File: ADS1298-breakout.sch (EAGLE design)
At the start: 33 parts, among them IC2 TPS73250DBVT, IC3 TPS73233DBVT

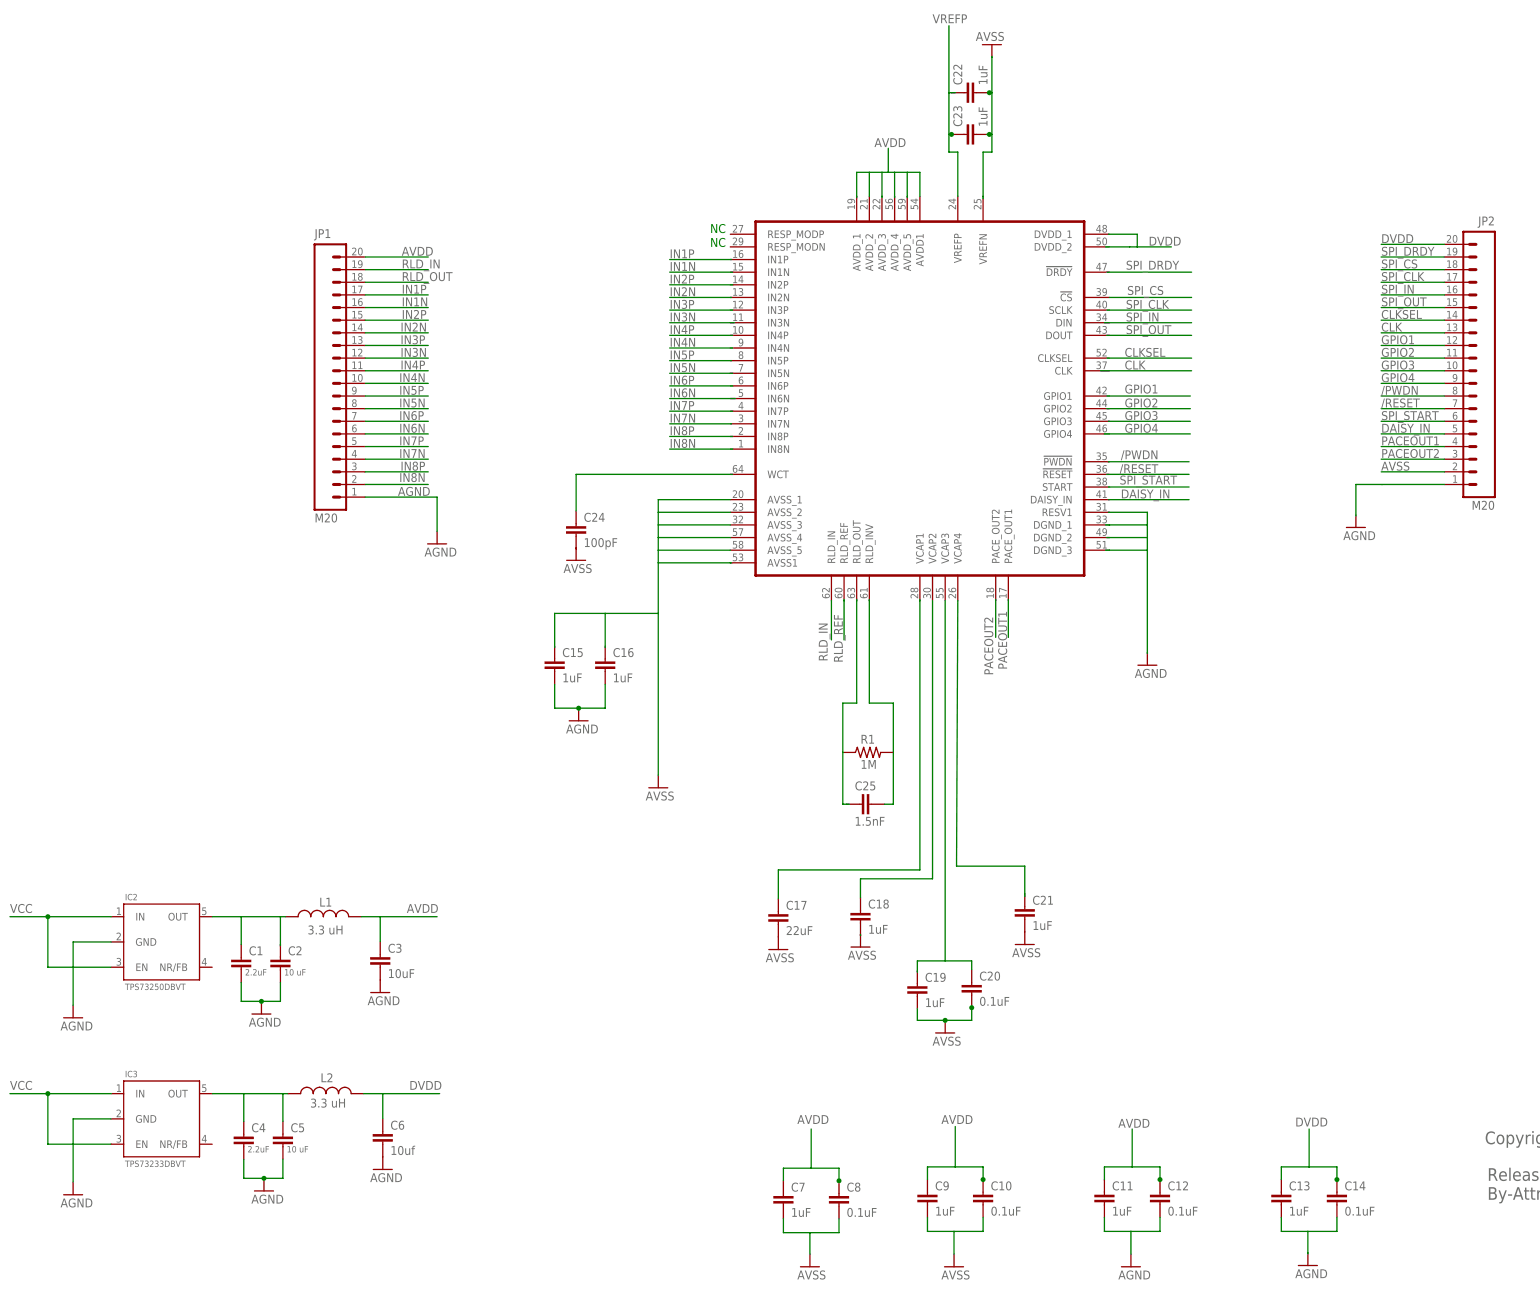
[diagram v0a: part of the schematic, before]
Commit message: schematic passes ERC
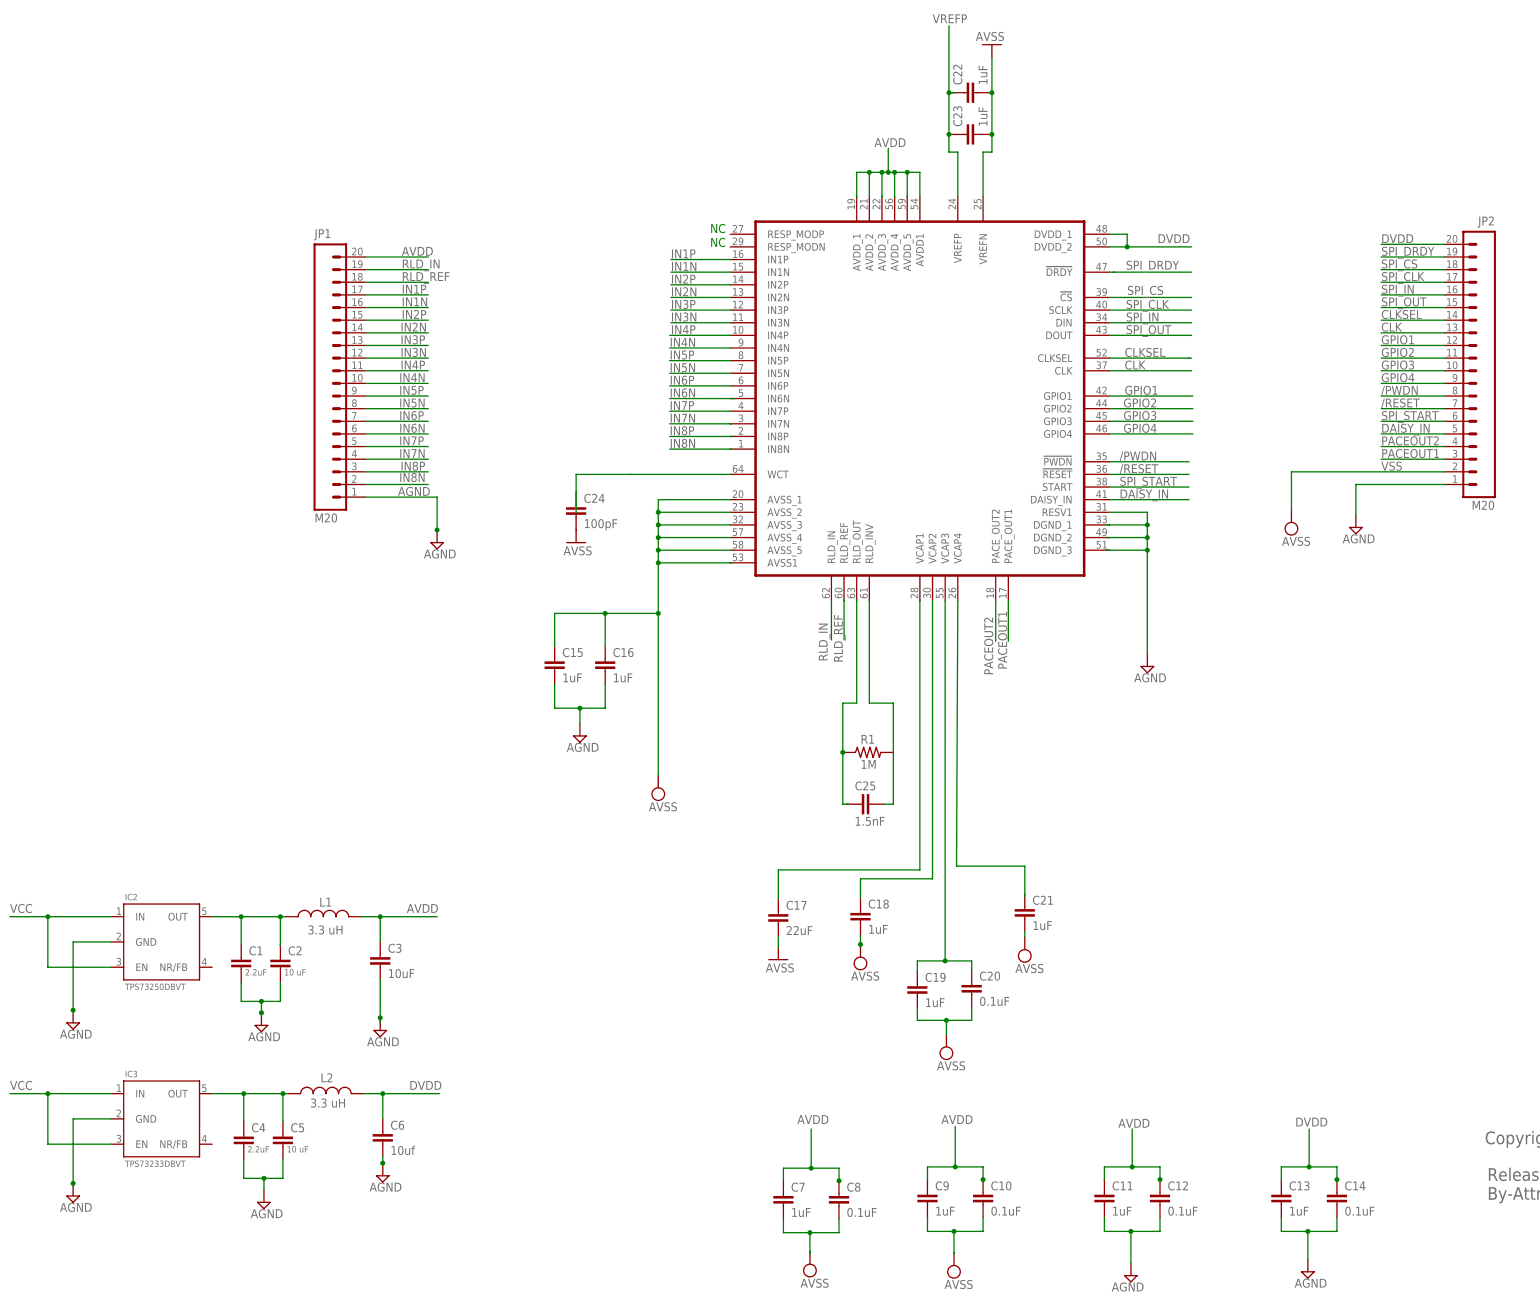
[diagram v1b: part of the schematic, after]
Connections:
- removed net AVSS: C10.2, C22.2, C23.2, C7.2, C8.2, C9.2, JP2.2, U$1.AVSS1, U$1.AVSS_1, U$1.AVSS_2, U$1.AVSS_3, U$1.AVSS_4, U$1.AVSS_5, U$1.VREFN
- removed net N$10: JP2.1
- removed net N$6: C19.1, C20.1
- new net VSS: C10.2, C15.1, C16.1, C18.2, C19.2, C20.2, C21.2, C7.2, C8.2, C9.2, JP2.2, U$1.AVSS1, U$1.AVSS_1, U$1.AVSS_2, U$1.AVSS_3, U$1.AVSS_4, U$1.AVSS_5
- net /PWDN: now also U$1.!PWDN
- net /RESET: now also U$1.!RESET
- net AGND: now also C15.2, C16.2, JP2.1, U$1.RESV1
- net CLK: now also U$1.CLK
- net CLKSEL: now also U$1.CLKSEL
- net DAISY_IN: now also U$1.DAISY_IN
- net DVDD: now also U$1.DVDD_1, U$1.DVDD_2
- net GND: now also C22.2, C23.2, C24.2, U$1.VREFN; no longer C15.2, C16.2, C18.2, C19.2, C20.2, C21.2
- net GPIO1: now also U$1.GPIO1
- net GPIO2: now also U$1.GPIO2
- net GPIO3: now also U$1.GPIO3
- net GPIO4: now also U$1.GPIO4
- net IN1N: now also U$1.IN1N
- net IN1P: now also U$1.IN1P
- net IN2N: now also U$1.IN2N
- net IN2P: now also U$1.IN2P
- net IN3N: now also U$1.IN3N
- net IN3P: now also U$1.IN3P
- net IN4N: now also U$1.IN4N
- net IN4P: now also U$1.IN4P
- net IN5N: now also U$1.IN5N
- net IN5P: now also U$1.IN5P
- net IN6N: now also U$1.IN6N
- net IN6P: now also U$1.IN6P
- net IN7N: now also U$1.IN7N
- net IN7P: now also U$1.IN7P
- net IN8N: now also U$1.IN8N
- net IN8P: now also U$1.IN8P
- net N$5: now also C19.1, C20.1
- net N$7: now also U$1.WCT
- net PACEOUT1: now also JP2.3, U$1.PACE_OUT1; no longer JP2.4
- net PACEOUT2: now also JP2.4, U$1.PACE_OUT2; no longer JP2.3
- net RLD_OUT: no longer JP1.18
- net RLD_REF: now also JP1.18
- net SPI_CLK: now also U$1.SCLK
- net SPI_DRDY: now also U$1.!DRDY
- net SPI_IN: now also U$1.DIN
- net SPI_OUT: now also U$1.DOUT
- net SPI_START: now also U$1.START
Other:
- moved on the sheet: C24

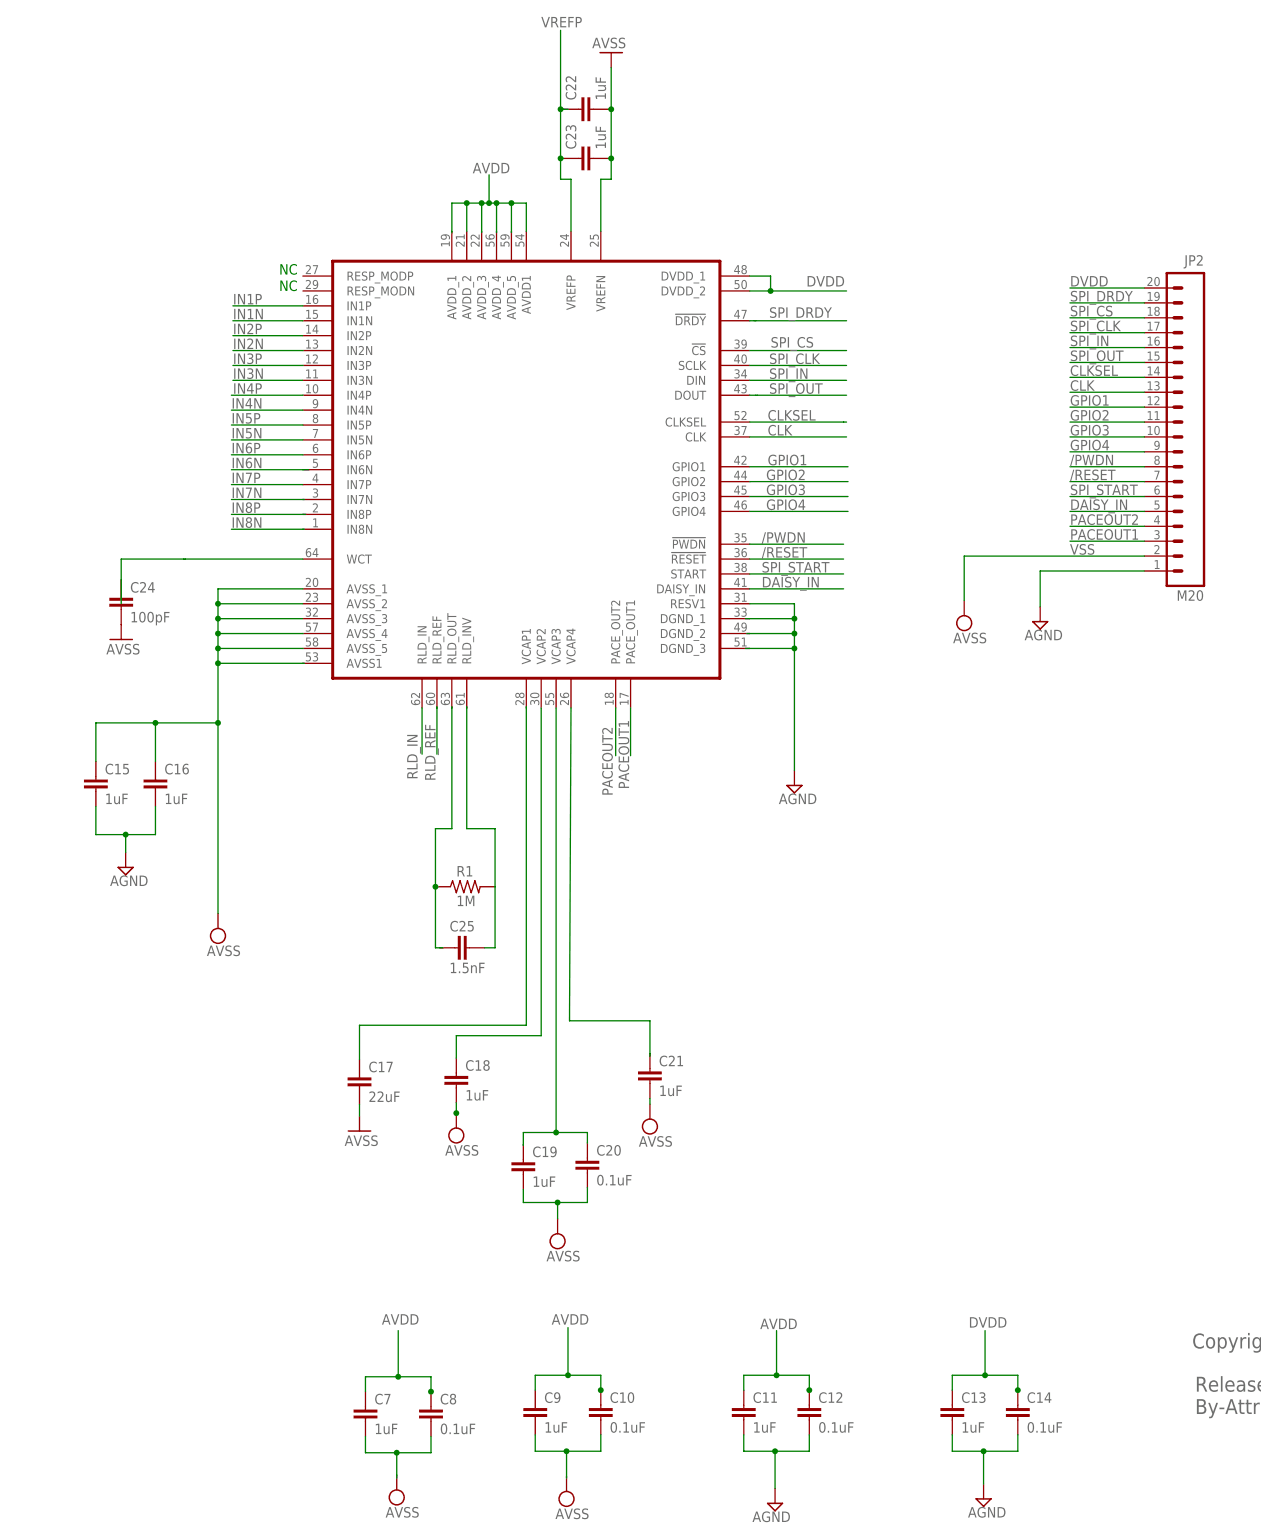
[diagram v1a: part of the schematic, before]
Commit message: changed pinout to facilate routing; board is still unrouted
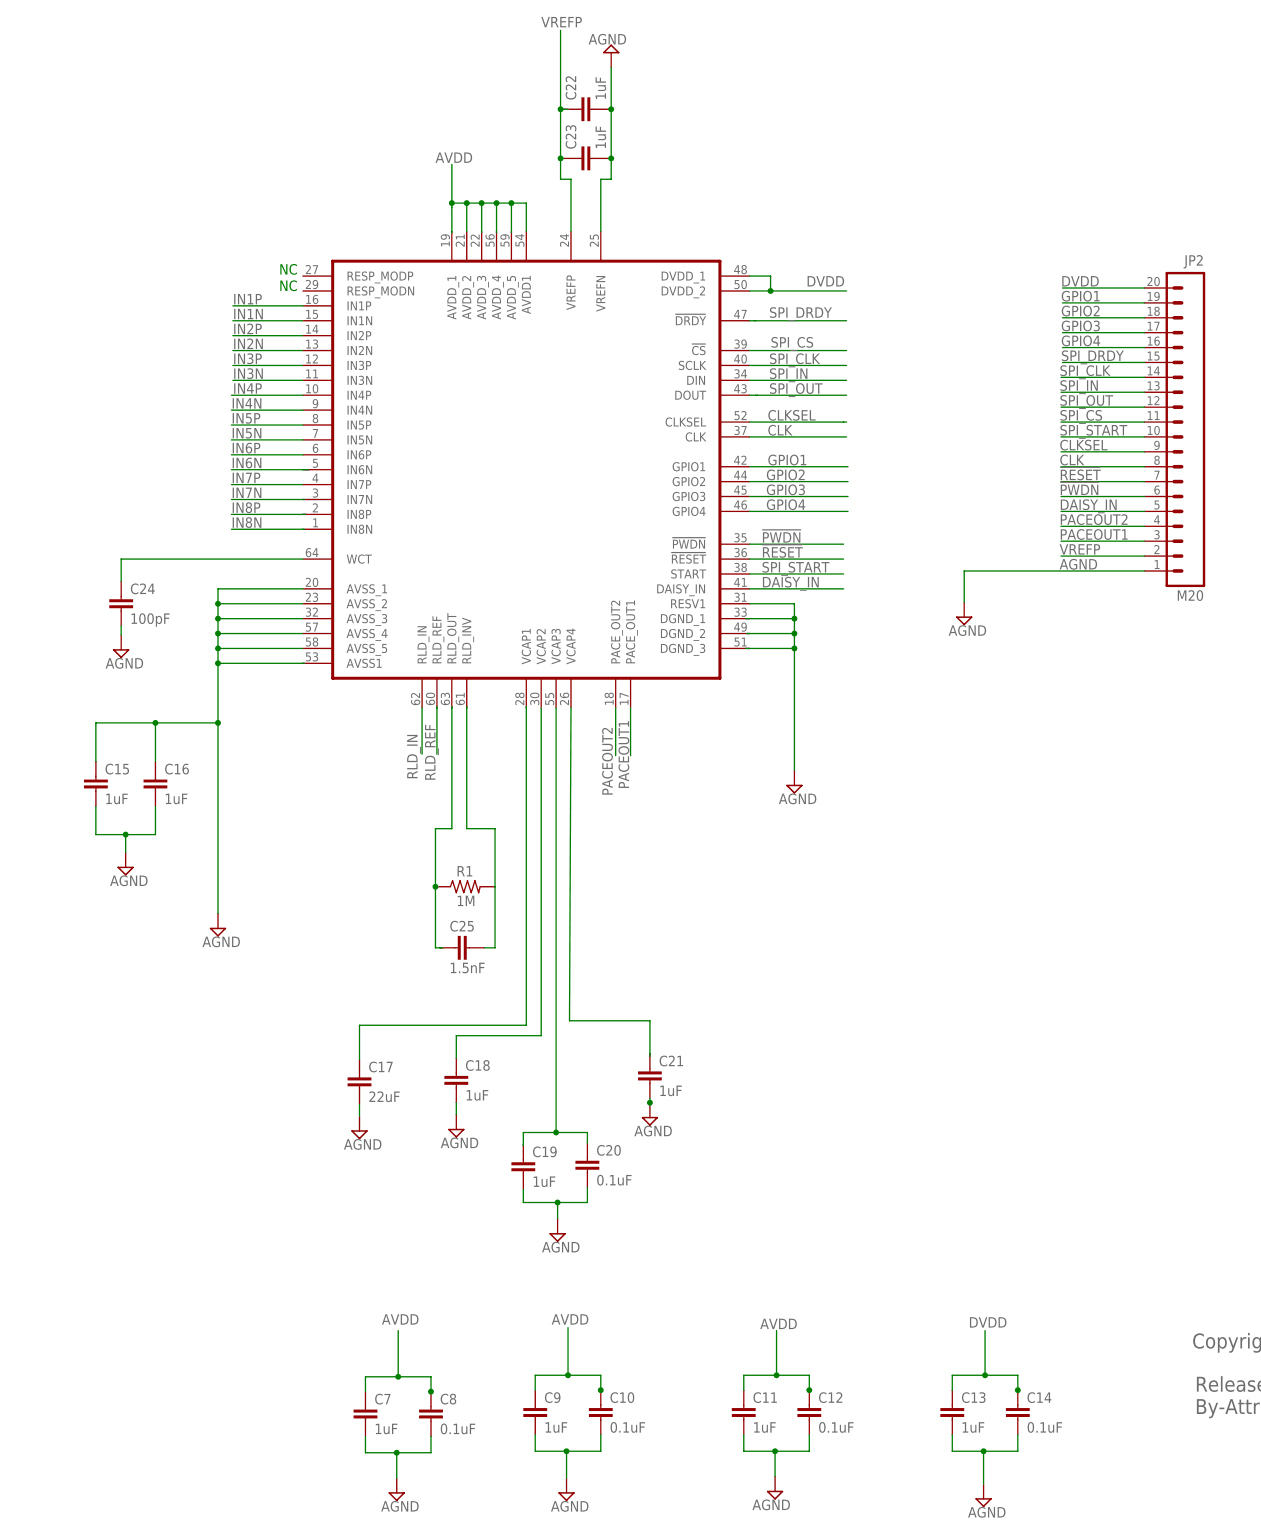
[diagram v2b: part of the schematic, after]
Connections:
- net /RESET renamed !RESET
- removed net /PWDN: JP2.8, U$1.!PWDN
- removed net GND: C17.2, C22.2, C23.2, C24.2, U$1.VREFN
- removed net VSS: C10.2, C15.1, C16.1, C18.2, C19.2, C20.2, C21.2, C7.2, C8.2, C9.2, JP2.2, U$1.AVSS1, U$1.AVSS_1, U$1.AVSS_2, U$1.AVSS_3, U$1.AVSS_4, U$1.AVSS_5
- new net !PWDN: JP2.6, U$1.!PWDN
- net AGND: now also C10.2, C15.1, C16.1, C17.2, C18.2, C19.2, C20.2, C21.2, C22.2, C23.2, C24.2, C7.2, C8.2, C9.2, U$1.AVSS1, U$1.AVSS_1, U$1.AVSS_2, U$1.AVSS_3, U$1.AVSS_4, U$1.AVSS_5, U$1.VREFN
- net CLK: now also JP2.8; no longer JP2.13
- net CLKSEL: now also JP2.9; no longer JP2.14
- net GPIO1: now also JP2.19; no longer JP2.12
- net GPIO2: now also JP2.18; no longer JP2.11
- net GPIO3: now also JP2.17; no longer JP2.10
- net GPIO4: now also JP2.16; no longer JP2.9
- net SPI_CLK: now also JP2.14; no longer JP2.17
- net SPI_CS: now also JP2.11; no longer JP2.18
- net SPI_DRDY: now also JP2.15; no longer JP2.19
- net SPI_IN: now also JP2.13; no longer JP2.16
- net SPI_OUT: now also JP2.12; no longer JP2.15
- net SPI_START: now also JP2.10; no longer JP2.6
- net VREFP: now also JP2.2

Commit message: corrected minor errors in schematic; changed from 20 to 24 pin headers; board partially routed
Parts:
- removed C15, C16: 1uF, SparkFun-Passives:CAP0603-CAP
- JP1, JP2: value M20 -> M24; device SparkFun-Connectors:M20 -> SparkFun-Connectors:M24
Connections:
- net !PWDN: now also JP2.9; no longer JP2.6
- net !RESET: now also JP2.10; no longer JP2.7
- net AGND: now also JP1.2, JP1.23, JP1.3, JP1.4, JP2.2, JP2.3, JP2.4; no longer C15.1, C15.2, C16.1, C16.2, JP1.1, JP2.1
- net AVDD: now also JP1.24, JP2.24; no longer JP1.20
- net CLK: now also JP2.11; no longer JP2.8
- net CLKSEL: now also JP2.12; no longer JP2.9
- net DAISY_IN: now also JP2.8; no longer JP2.5
- net DVDD: now also JP2.23; no longer JP2.20
- net GPIO1: now also JP2.22; no longer JP2.19
- net GPIO2: now also JP2.21; no longer JP2.18
- net GPIO3: now also JP2.20; no longer JP2.17
- net GPIO4: now also JP2.19; no longer JP2.16
- net IN1N: now also JP1.19; no longer JP1.16
- net IN1P: now also JP1.20; no longer JP1.17
- net IN2N: now also JP1.17; no longer JP1.14
- net IN2P: now also JP1.18; no longer JP1.15
- net IN3N: now also JP1.15; no longer JP1.12
- net IN3P: now also JP1.16; no longer JP1.13
- net IN4N: now also JP1.13; no longer JP1.10
- net IN4P: now also JP1.14; no longer JP1.11
- net IN5N: now also JP1.11; no longer JP1.8
- net IN5P: now also JP1.12; no longer JP1.9
- net IN6N: now also JP1.9; no longer JP1.6
- net IN6P: now also JP1.10; no longer JP1.7
- net IN7N: now also JP1.7; no longer JP1.4
- net IN7P: now also JP1.8; no longer JP1.5
- net IN8N: now also JP1.5; no longer JP1.2
- net IN8P: now also JP1.6; no longer JP1.3
- net PACEOUT1: now also JP2.6; no longer JP2.3
- net PACEOUT2: now also JP2.7; no longer JP2.4
- net RLD_IN: now also JP1.22; no longer JP1.19
- net RLD_REF: now also JP1.21; no longer JP1.18
- net SPI_CLK: now also JP2.17; no longer JP2.14
- net SPI_CS: now also JP2.14; no longer JP2.11
- net SPI_DRDY: now also JP2.18; no longer JP2.15
- net SPI_IN: now also JP2.16; no longer JP2.13
- net SPI_OUT: now also JP2.15; no longer JP2.12
- net SPI_START: now also JP2.13; no longer JP2.10
- net VCC: now also JP1.25, JP2.25
- net VREFP: now also JP2.5; no longer JP2.2

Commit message: changed via drill holes to be 0.020 inch, compatible with AP Circuits
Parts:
- renumbered U$1 to IC1

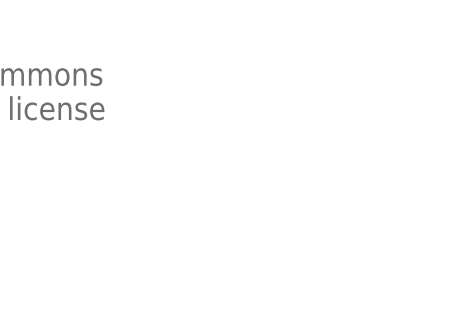
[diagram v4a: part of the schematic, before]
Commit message: top silkscreen has pin numbers and functions; board name and version; OSH logo; and CC-BY-SA license
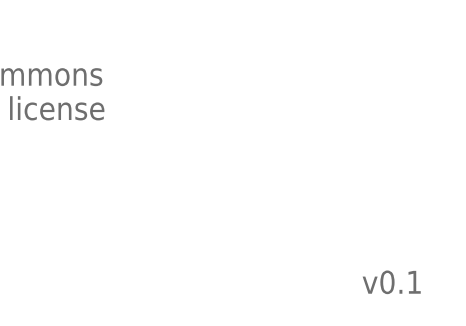
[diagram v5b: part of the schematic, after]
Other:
- note added: "v0.1"
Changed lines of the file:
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@@
 By-Attribution Share-Alike 3.0 license</text>
 <text x="328.676" y="37.592" size="2.54" layer="95">Copyright 2013 Adam Feuer</text>
+<text x="416.306" y="7.112" size="2.54" layer="95">v0.1</text>
 </plain>
 <instances>
